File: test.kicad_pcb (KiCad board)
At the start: 4 copper layers, 100 x 48 mm, 108 parts, among them IC1 USBLC6-2SC6, IC2 ESP32-S3-WROOM-1-N16, IC3 MAX17048G+T10, IC4 BQ24074RGTR, IC5 LM4041CEM3-ADJ_NOPB, IC8 DAC5571IDBVR, IC9 DAC5571IDBVR, J1 PWM, J2 UART0, SW1 Reset, SW2 Button, SW3 SW_DPDT_x2, U1 USB-C_SMD-TYPE-C-31-M-12, U2 ADC08351CILQX/NOPB, U3 ADC08351CILQX/NOPB, U4 1043, U5 1043, U6 LD1086DT33TR, U7 LD1086DT33TR

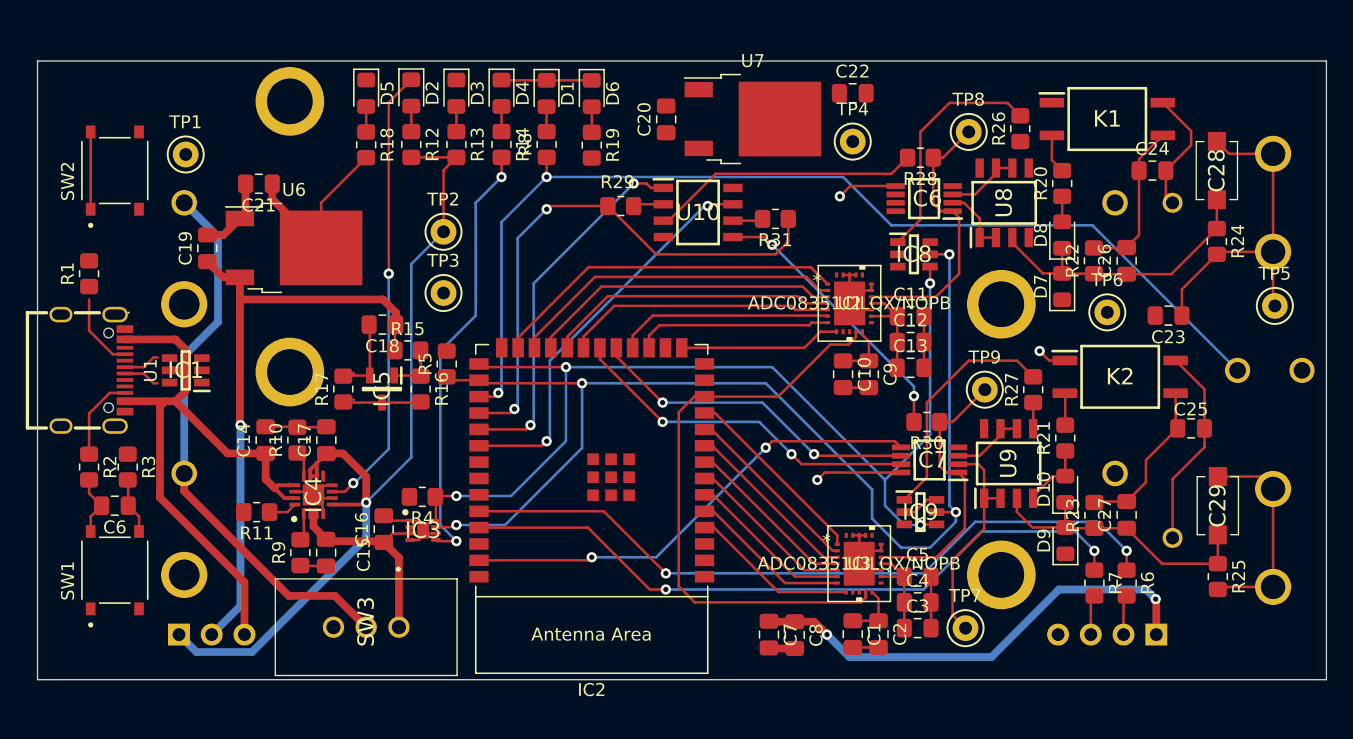
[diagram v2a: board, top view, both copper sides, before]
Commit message: Added ADC vor Trigger and changed Layout
Some Traces cant be good routed
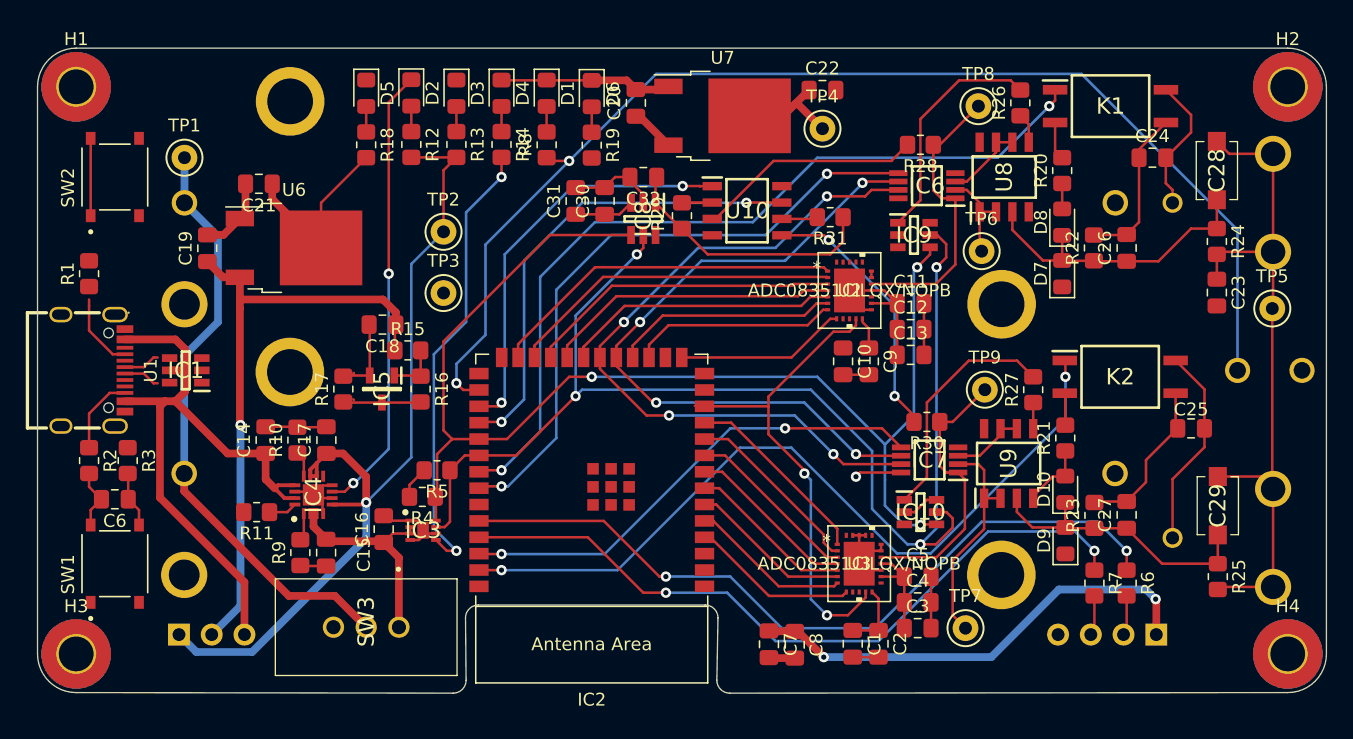
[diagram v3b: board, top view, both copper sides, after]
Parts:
- added C30: 10u, Capacitor_SMD:C_0805_2012Metric_Pad1.18x1.45mm_HandSolder, F.Cu at (144.0, 60.9)
- added C31: 0.1u, Capacitor_SMD:C_0805_2012Metric_Pad1.18x1.45mm_HandSolder, F.Cu at (141.8, 60.9)
- added C32: 0.1u, Capacitor_SMD:C_0805_2012Metric_Pad1.18x1.45mm_HandSolder, F.Cu at (147.0, 59.0)
- added H1: MountingHole, MountingHole:MountingHole_2.7mm_Pad_TopBottom, F.Cu at (103.0, 52.0)
- added H2: MountingHole, MountingHole:MountingHole_2.7mm_Pad_TopBottom, F.Cu at (197.0, 52.0)
- added H3: MountingHole, MountingHole:MountingHole_2.7mm_Pad_TopBottom, F.Cu at (103.0, 96.0)
- added H4: MountingHole, MountingHole:MountingHole_2.7mm_Pad_TopBottom, F.Cu at (197.0, 96.0)
- added IC8: MCP4726A0T-E_CH, project_library:MCP4726A1T-E_CH, F.Cu at (147.0, 62.2)
- IC6, IC7: value ~ -> MCP6S91-E_MS
- K1, K2: value ~ -> AQY210EHAX
- U10, U8, U9: value ~ -> MCP6022T-I_SN
- moved TP6 10.8 mm to (173.2, 64.8)
- moved R5 8.28 mm to (131.0, 81.8), turned to 180 degrees
- moved R29 4.81 mm to (150.0, 62.0), turned to 90 degrees
- moved R31 4.25 mm to (161.5, 62.1)
- moved C23 4.15 mm to (191.5, 68.0), turned to -90 degrees
- moved U10 3.80 mm to (155.1, 61.6)
- moved C20 2.67 mm to (146.4, 53.2)
- moved TP4 2.55 mm to (160.9, 55.2)
- moved C22 2.36 mm to (160.9, 52.2)
- moved U7 2.36 mm to (153.2, 54.2)
- moved TP8 2.14 mm to (173.0, 53.5)
- moved R26 2.00 mm to (176.2, 53.2)
- moved U8 2.00 mm to (175.0, 59.0)
- moved IC9 1.50 mm to (168.0, 63.5)
- moved K1 1.03 mm to (183.2, 53.5)
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- renumbered IC9 to IC10, IC8 to IC9
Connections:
- IC2 pad 27: SDA -> Net-(IC2-Pad27)
- IC2 pad 28: SCL_I2C -> /Status_PWM
- IC2 pad 29: /Status_PWM -> Trigger_CH1
- IC2 pad 30: Trigger_Ref -> Trigger_CH2
- IC2 pad 31: Trigger_CH1 -> SDA
- IC2 pad 32: Trigger_CH2 -> SCL_I2C
- IC2 pad 34: CH2_AC_Sel -> CS_Gain_CH1
- IC2 pad 38: CS_Gain_CH1 -> CS_Gain_CH2
- IC2 pad 39: CS_Gain_CH2 -> CH2_AC_Sel
- R29 pad 1: Trigger_Ref -> Net-(C32-Pad1)
- R31 pad 1: Trigger_Ref -> Net-(C32-Pad1)
- SW2 pad A: SDA -> Net-(IC2-Pad27)
- SW2 pad B: SDA -> Net-(IC2-Pad27)
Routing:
- net CH1_AC_Sel: track 0.00 -> 64.5 mm, vias 0 -> 2
- net CH2_AC_Sel: track 2.25 -> 61.7 mm, vias 1 -> 2
- net CS_Gain_CH1: track 4.66 -> 49.4 mm, vias 1 -> 2
- net Trigger_Ref: track 42.0 -> 0.00 mm, vias 2 -> 0
- net SCLK_SPI: track 27.6 -> 56.2 mm, vias 2 -> 4
- net MOSI: track 25.9 -> 53.5 mm, vias 2 -> 4
- net Net-(C32-Pad1): track 0.00 -> 20.2 mm
- net +3.3VA: track 24.6 -> 40.3 mm
- net /Status_PWM: track 81.3 -> 95.3 mm
- net SDA: track 85.6 -> 96.6 mm, vias 4 -> 3
- net GNDREF: track 48.7 -> 58.7 mm
- net GND: track 73.2 -> 83.2 mm
- net /I2S_CLK: track 45.7 -> 38.1 mm, vias 0 -> 2
- net SCL_I2C: track 90.0 -> 97.3 mm
- net Trigger_CH2: track 31.0 -> 37.6 mm
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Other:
- board size 100 x 48 mm -> 100 x 50 mm

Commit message: new idear to arange gnd ref in layout
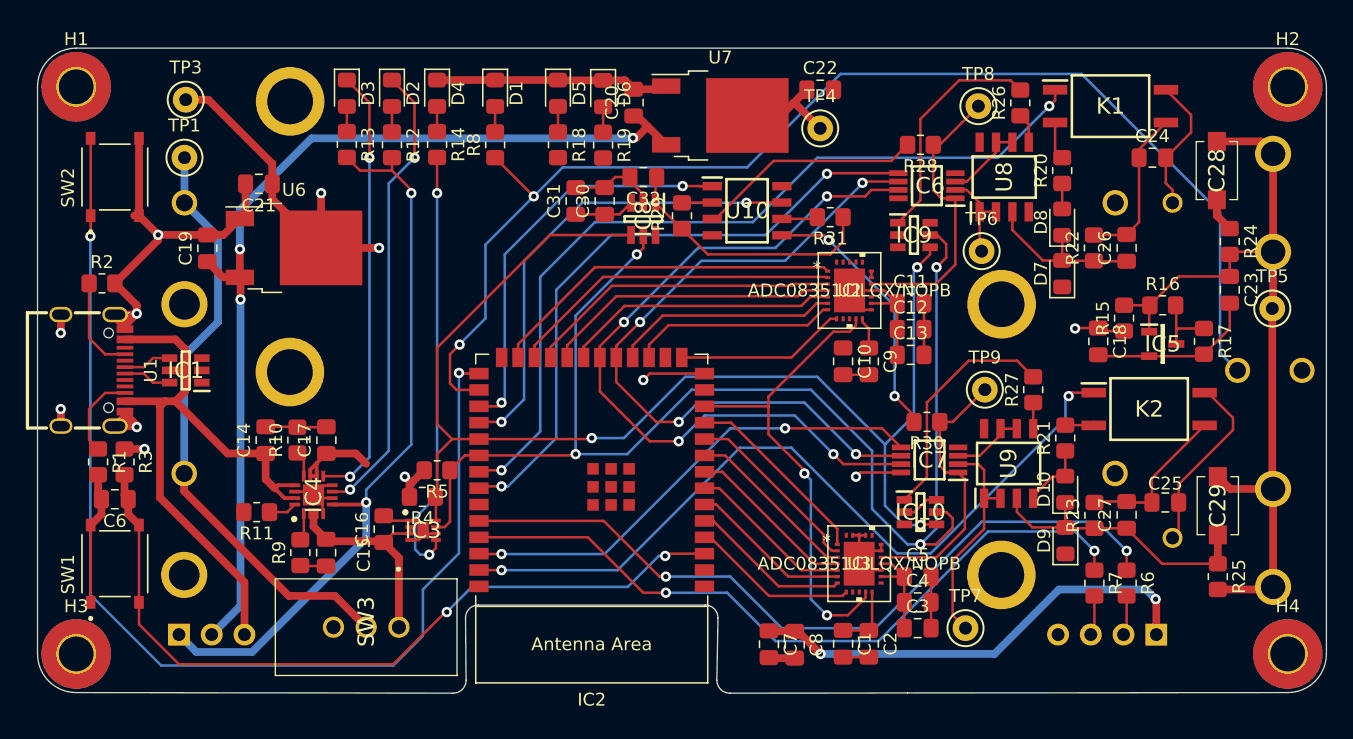
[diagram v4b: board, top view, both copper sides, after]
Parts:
- removed TP2: VBatChargeIC, TestPoint:TestPoint_Keystone_5000-5004_Miniature
- U1: value USB-C_SMD-TYPE-C-31-M-12 -> USB-TYPE-C-018
- moved R17 66.9 mm to (190.5, 71.8), turned to -90 degrees
- moved IC5 60.7 mm to (187.3, 72.0), turned to 0 degrees
- moved R16 57.9 mm to (187.3, 69.0), turned to 0 degrees
- moved R15 55.6 mm to (184.3, 70.0), turned to 90 degrees
- moved C18 55.6 mm to (182.3, 71.8), turned to -90 degrees
- moved TP3 25.0 mm to (111.5, 53.0)
- moved D5 14.9 mm to (140.4, 52.5)
- moved R18 14.9 mm to (140.4, 56.5)
- moved R1 14.6 mm to (104.7, 81.1), turned to -90 degrees
- moved R2 13.8 mm to (105.0, 67.2), turned to 0 degrees
- moved D3 8.50 mm to (124.0, 52.5)
- moved R13 8.50 mm to (124.0, 56.5)
- moved C25 6.09 mm to (187.5, 84.2)
- moved D4 5.00 mm to (131.0, 52.5)
- moved R14 5.00 mm to (131.0, 56.5)
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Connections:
- IC1 pad 4: /D+ -> Net-(IC1-Pad4)
- IC1 pad 6: /D- -> Net-(IC1-Pad6)
- SW1 pad A: unconnected-(SW1-PadA) -> GND
- SW1 pad C: unconnected-(SW1-PadC) -> /ENABLE
- U1 pad 0: Net-(R1-Pad1) -> GND
- U1 pad 1: Net-(R1-Pad1) -> GND
- U1 pad 2: Net-(R1-Pad1) -> GND
- U1 pad 3: Net-(R1-Pad1) -> GND
- U1 pad A5: Net-(R4-Pad1) -> Net-(R2-Pad1)
- U1 pad A6: Net-(IC2-Pad4) -> Net-(IC1-Pad4)
- U1 pad A7: Net-(IC2-Pad6) -> Net-(IC1-Pad6)
- U1 pad B5: Net-(R2-Pad1) -> Net-(R1-Pad1)
- U1 pad B6: Net-(IC2-Pad4) -> Net-(IC1-Pad4)
- U1 pad B7: Net-(IC2-Pad6) -> Net-(IC1-Pad6)
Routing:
- net Net-(IC2-Pad27): track 6.35 -> 87.9 mm, vias 0 -> 2
- net /ENABLE: track 4.36 -> 61.2 mm, vias 0 -> 2
- net +3V3: track 61.1 -> 113.6 mm, vias 2 -> 6
- net GND: track 83.2 -> 128.0 mm, vias 0 -> 5
- net Charging: track 0.00 -> 34.2 mm, vias 0 -> 2
- net Net-(C18-Pad1): track 50.9 -> 79.0 mm, vias 1 -> 4
- net Net-(C26-Pad1): track 23.5 -> 15.9 mm
- net GNDA: track 8.02 -> 15.1 mm
- net Net-(R1-Pad1): track 0.00 -> 6.69 mm
- net GNDREF: track 58.7 -> 65.3 mm
- net Net-(R4-Pad1): track 5.96 -> 0.00 mm
- net /USB_D+: track 0.00 -> 4.96 mm, vias 0 -> 1
- net SCL_I2C: track 97.3 -> 102.0 mm
- net Net-(IC1-Pad6): track 0.00 -> 3.76 mm
- net Net-(IC1-Pad4): track 0.00 -> 3.76 mm
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- added copper zone on In2.Cu, net +3.3VA
- added copper zone on In2.Cu, net +3V3
- removed copper zone on In2.Cu, net GND
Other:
- outline, holes or cut-outs redrawn

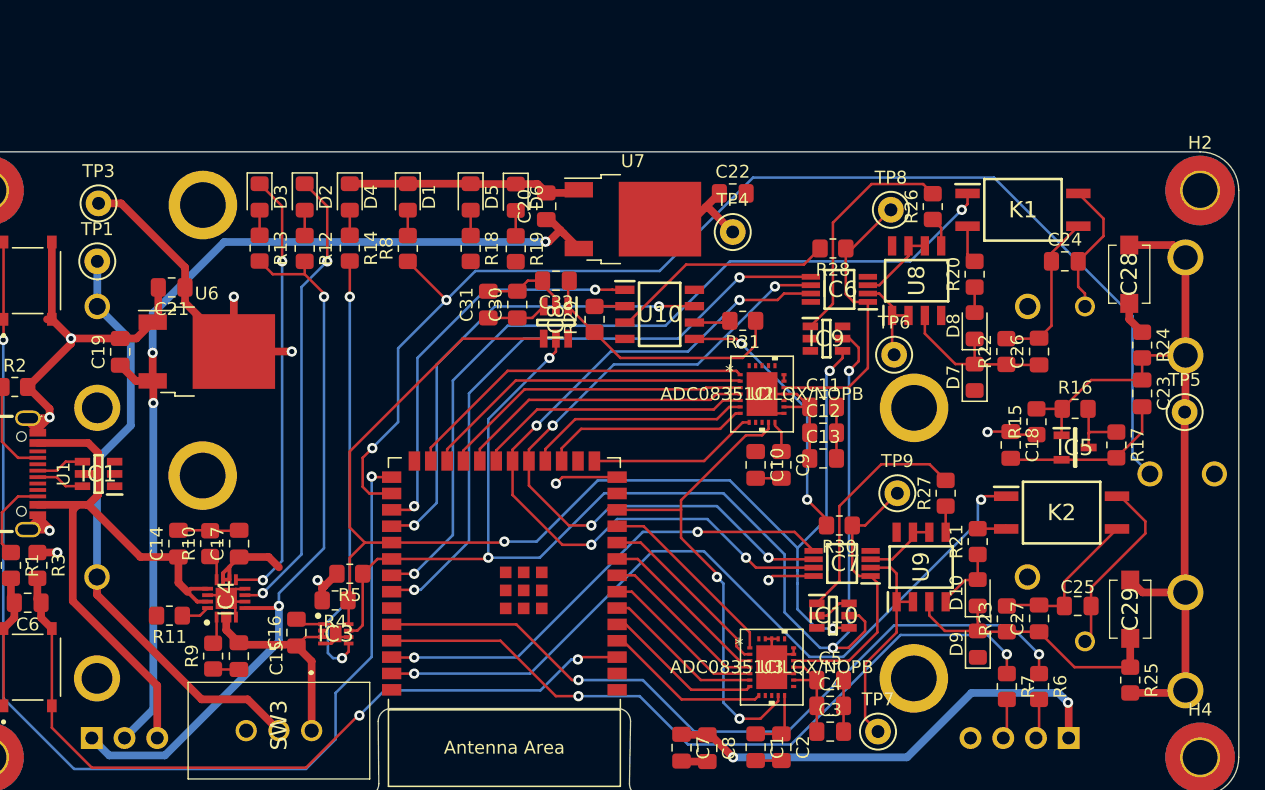
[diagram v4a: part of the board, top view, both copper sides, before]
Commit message: added values for analog front end
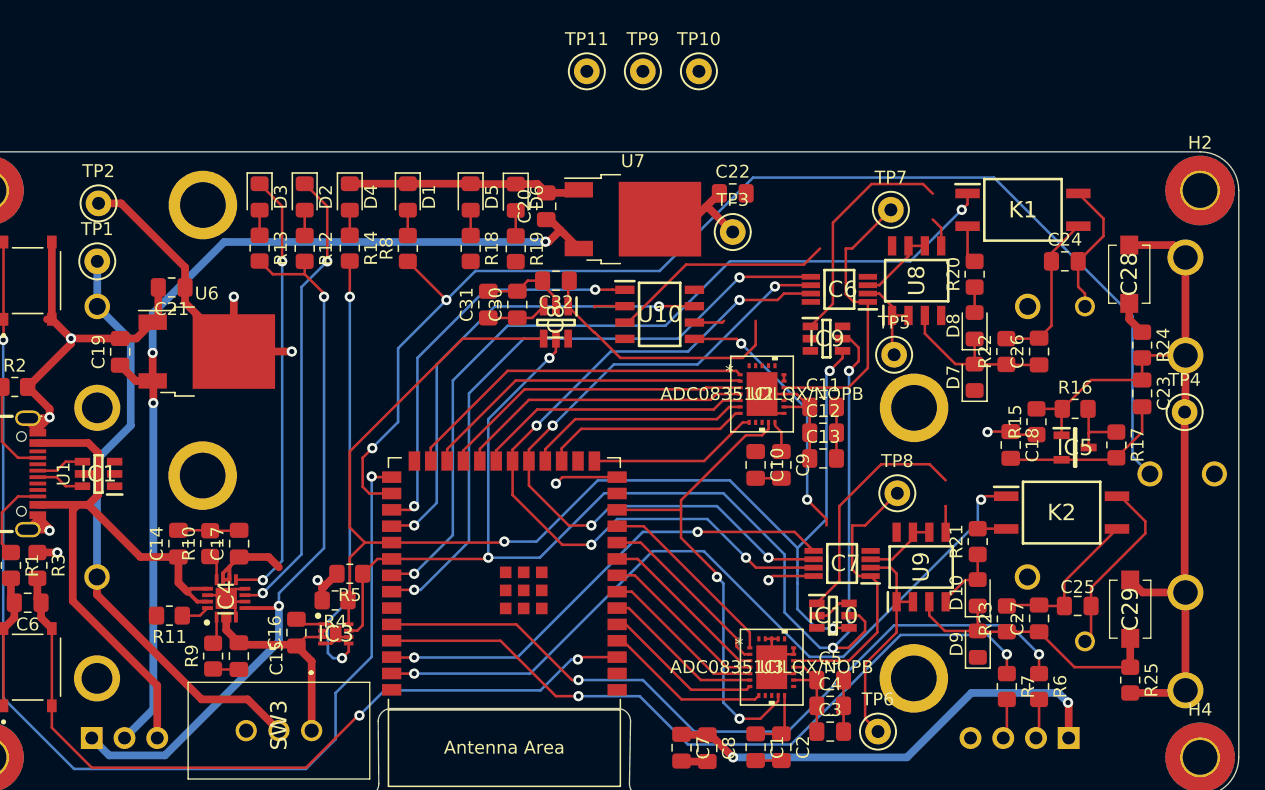
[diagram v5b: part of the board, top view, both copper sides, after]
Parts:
- removed R26, R27, R28, R29, R30, R31: ~, Resistor_SMD:R_0805_2012Metric_Pad1.20x1.40mm_HandSolder
- added TP10: ?, TestPoint:TestPoint_Keystone_5000-5004_Miniature, F.Cu at (158.1, 42.8)
- added TP11: ?, TestPoint:TestPoint_Keystone_5000-5004_Miniature, F.Cu at (149.4, 42.8)
- added TP9: ?, TestPoint:TestPoint_Keystone_5000-5004_Miniature, F.Cu at (153.8, 42.8)
- C24, C25: value ~ -> 100n
- C26, C27: value ~ -> 5p
- C28, C29: value ~ -> Var_25p
- D10, D7, D8, D9: value ~ -> D_Schottky
- R20, R21: value ~ -> 1k
- R22, R23: value ~ -> 835k
- R24, R25: value ~ -> 165k
- renumbered TP3 to TP2, TP4 to TP3, TP5 to TP4, TP6 to TP5, TP7 to TP6, TP8 to TP7, TP9 to TP8
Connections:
- U10 pad 2: Net-(R29-Pad2) -> Net-(C32-Pad1)
- U10 pad 3: Net-(R28-Pad2) -> Analog_Out_CH1
- U10 pad 5: Net-(R30-Pad2) -> Analog_Out_CH2
- U10 pad 6: Net-(R31-Pad2) -> Net-(C32-Pad1)
- U8 pad 5: Net-(R26-Pad1) -> /Analog/Offset_CH1
- U9 pad 5: Net-(R27-Pad1) -> /Analog/Offset_CH2
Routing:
- net Net-(R30-Pad2): track 20.6 -> 0.00 mm, vias 2 -> 0
- net Analog_Out_CH2: track 21.6 -> 42.2 mm, vias 0 -> 2
- net Net-(R28-Pad2): track 18.4 -> 0.00 mm
- net Analog_Out_CH1: track 22.5 -> 40.9 mm
- net Net-(C32-Pad1): track 20.2 -> 25.0 mm
- net Net-(R29-Pad2): track 2.42 -> 0.00 mm
- net Net-(R31-Pad2): track 2.36 -> 0.00 mm
- net /Analog/Offset_CH1: track 18.1 -> 20.4 mm
- net Net-(R26-Pad1): track 2.32 -> 0.00 mm
- net /Analog/Offset_CH2: track 18.4 -> 20.4 mm
- net Net-(R27-Pad1): track 2.03 -> 0.00 mm
